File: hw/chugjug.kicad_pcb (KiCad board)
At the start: 4 copper layers, 50 x 50 mm, 42 parts, among them J1 SAMTEC_FTSH-107-01-L-DV-K-A, J2 BATT_IN_JST, J4 USB2.0 TYPE-C 6P SMD, U1 STM32U575RITxQ, U2 MCP73833-xxx-UN, U3 LIS3DH, U4 MAX98357A, U5 TPS78233DDCR

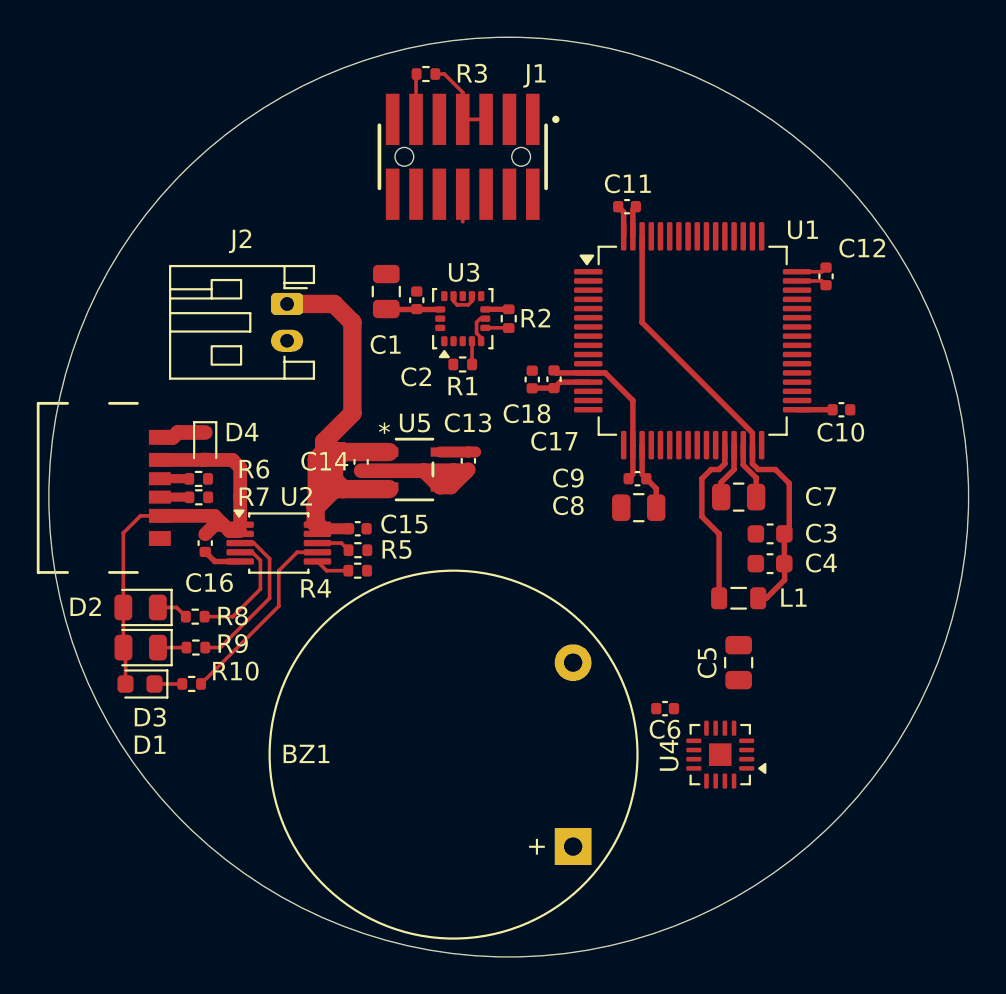
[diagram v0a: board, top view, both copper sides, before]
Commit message: much more layout changes. amp powered from +batt now
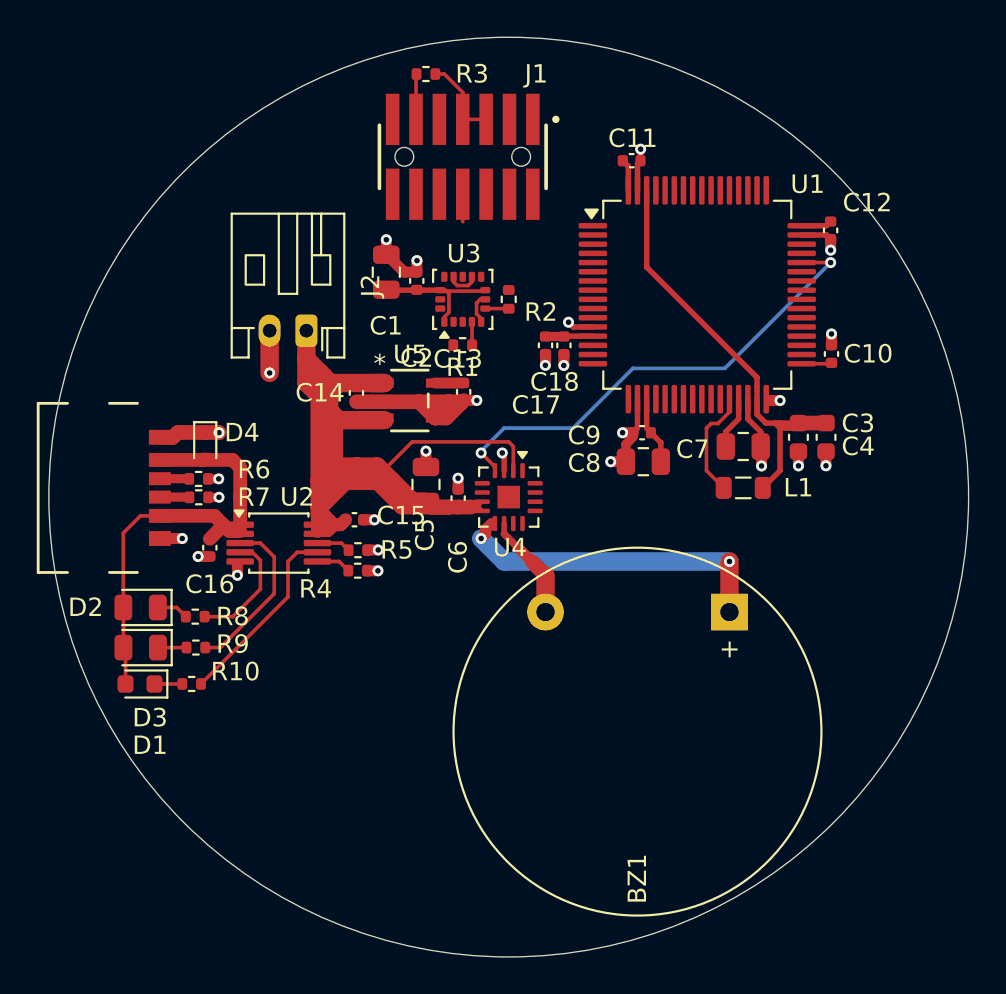
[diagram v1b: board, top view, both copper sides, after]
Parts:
- moved C5 19.6 mm to (145.5, 99.3)
- moved U4 18.1 mm to (150.0, 100.0), turned to -90 degrees
- moved C6 16.0 mm to (147.2, 100.1), turned to 90 degrees
- moved BZ1 15.3 mm to (162.0, 106.2), turned to 180 degrees
- moved C4 7.51 mm to (167.2, 96.8), turned to -90 degrees
- moved L1 6.01 mm to (162.8, 99.5)
- moved C3 5.47 mm to (165.8, 96.8), turned to -90 degrees
- moved C13 3.76 mm to (147.5, 94.3)
- moved C14 3.76 mm to (141.7, 94.3)
- moved U5 3.76 mm to (144.6, 94.8)
- moved C10 3.08 mm to (167.5, 92.2), turned to -90 degrees
- moved C7 2.76 mm to (162.8, 97.2)
- moved C18 2.53 mm to (153.0, 91.8), turned to 90 degrees
- moved C11 2.51 mm to (156.7, 81.7)
- moved C12 2.51 mm to (167.5, 85.5)
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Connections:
- C5 pad 1: 3V3 -> +BATT
- C5 pad 2: Net-(U4-GAIN_SLOT) -> GND
- C6 pad 1: 3V3 -> +BATT
- C6 pad 2: Net-(U4-GAIN_SLOT) -> GND
- U4 pad 2: Net-(U4-GAIN_SLOT) -> +BATT
- U4 pad 7: Net-(U4-GAIN_SLOT) -> +BATT
- U4 pad 8: Net-(U4-GAIN_SLOT) -> +BATT
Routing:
- net +BATT: track 29.9 -> 64.8 mm
- net /SD_MODE: track 0.00 -> 26.2 mm, vias 0 -> 2
- net Net-(BZ1-+): track 0.00 -> 18.1 mm, vias 0 -> 2
- net GND: track 38.4 -> 55.3 mm, vias 0 -> 28
- net Net-(BZ1--): track 0.00 -> 5.74 mm
- net /VLXSMPS: track 9.49 -> 5.95 mm
- net 3V3: track 21.0 -> 23.4 mm
- net /VDD11: track 24.5 -> 23.5 mm
- added copper zone on In2.Cu, net 3V3
- added copper zone on In1.Cu, net GND

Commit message: initial layout done
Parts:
- added REF**: MountingHole_2.2mm_M2, MountingHole:MountingHole_2.2mm_M2, F.Cu at (171.0, 96.2)
- added REF**: MountingHole_2.2mm_M2, MountingHole:MountingHole_2.2mm_M2, F.Cu at (131.2, 90.0)
- added REF**: MountingHole_2.2mm_M2, MountingHole:MountingHole_2.2mm_M2, F.Cu at (144.5, 120.8)
- moved R5 7.78 mm to (137.8, 96.2), turned to 180 degrees
- moved C16 5.46 mm to (135.2, 97.5), turned to 90 degrees
- moved U2 3.81 mm to (139.0, 99.0)
- moved C15 2.73 mm to (142.8, 98.8), turned to -90 degrees
- moved R4 2.56 mm to (141.2, 101.5), turned to 180 degrees
- moved R3 2.31 mm to (143.4, 77.8), turned to 90 degrees
- moved J1 1.60 mm to (148.8, 80.5)
- moved R2 1.05 mm to (149.9, 90.3), turned to 90 degrees
- moved R10 0.34 mm to (132.8, 110.5)
- moved D1 0.34 mm to (130.0, 110.5)
- moved C1 0.25 mm to (143.1, 87.8)
- moved C2 0.25 mm to (144.8, 88.2)
- moved D3 0.20 mm to (130.0, 108.4)
- moved R9 0.20 mm to (133.0, 108.4)
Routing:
- net /I2S_LRCLK: track 0.00 -> 27.8 mm, vias 0 -> 2
- net /STLINK_SWCLK: track 0.00 -> 24.8 mm, vias 0 -> 2
- net /LIS3DH_I2C1_SCL: track 1.27 -> 26.1 mm, vias 0 -> 2
- net /STLINK_SWO: track 1.50 -> 26.3 mm, vias 0 -> 2
- net /STLINK_SWDIO: track 0.00 -> 24.7 mm
- net /I2S_DATA: track 0.00 -> 24.0 mm, vias 0 -> 2
- net /LIS3DH_INT1: track 0.00 -> 22.2 mm, vias 0 -> 2
- net /I2S_BCLK: track 0.00 -> 22.0 mm, vias 0 -> 2
- net +BATT: track 64.8 -> 46.0 mm
- net /PWR_WKUP1: track 0.00 -> 17.8 mm
- net /STLINK_UART_RX: track 0.00 -> 17.4 mm, vias 0 -> 2
- net /LIS3DH_I2C1_SDA: track 1.28 -> 16.7 mm, vias 0 -> 2
- net /STLINK_UART_TX: track 0.00 -> 14.1 mm
- net /STLINK_NRST: track 0.00 -> 12.3 mm
- net 3V3: track 23.4 -> 35.5 mm, vias 0 -> 13
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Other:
- board text added: "CHG"
- board text added: "FULL"
- board text added: "PWR"

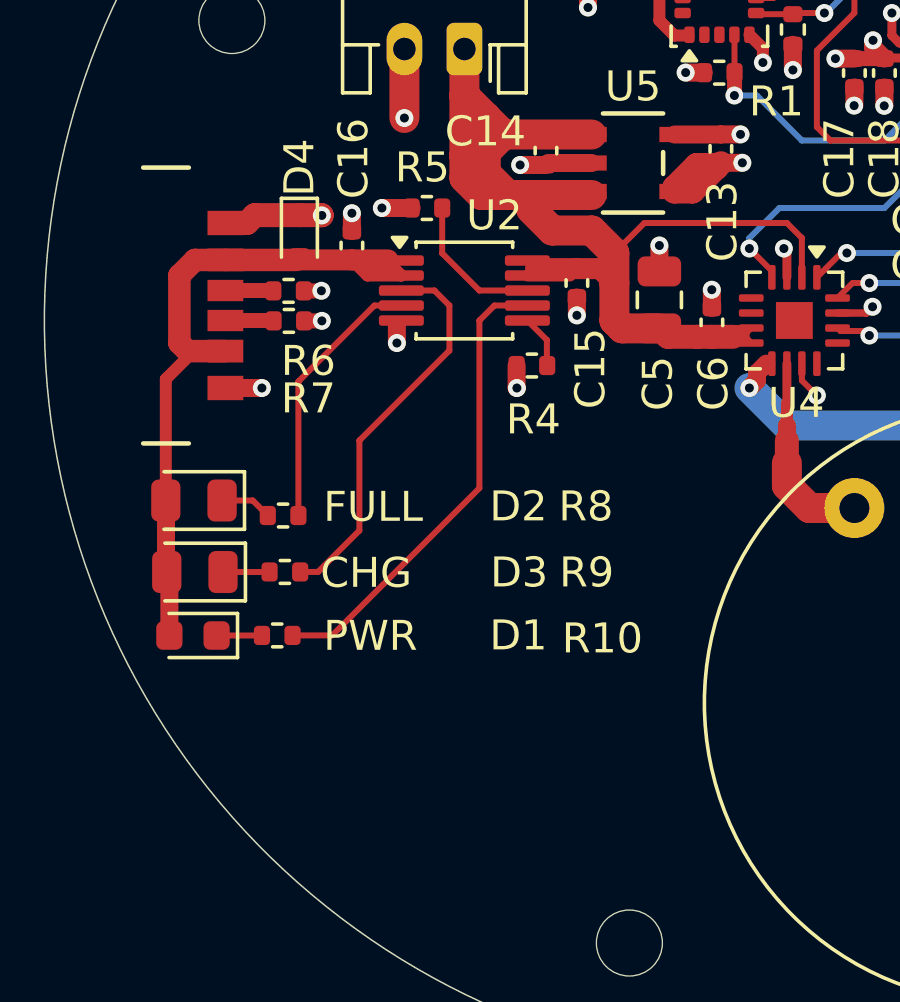
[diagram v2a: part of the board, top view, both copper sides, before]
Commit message: finalize pcb for jlcpcb ordering
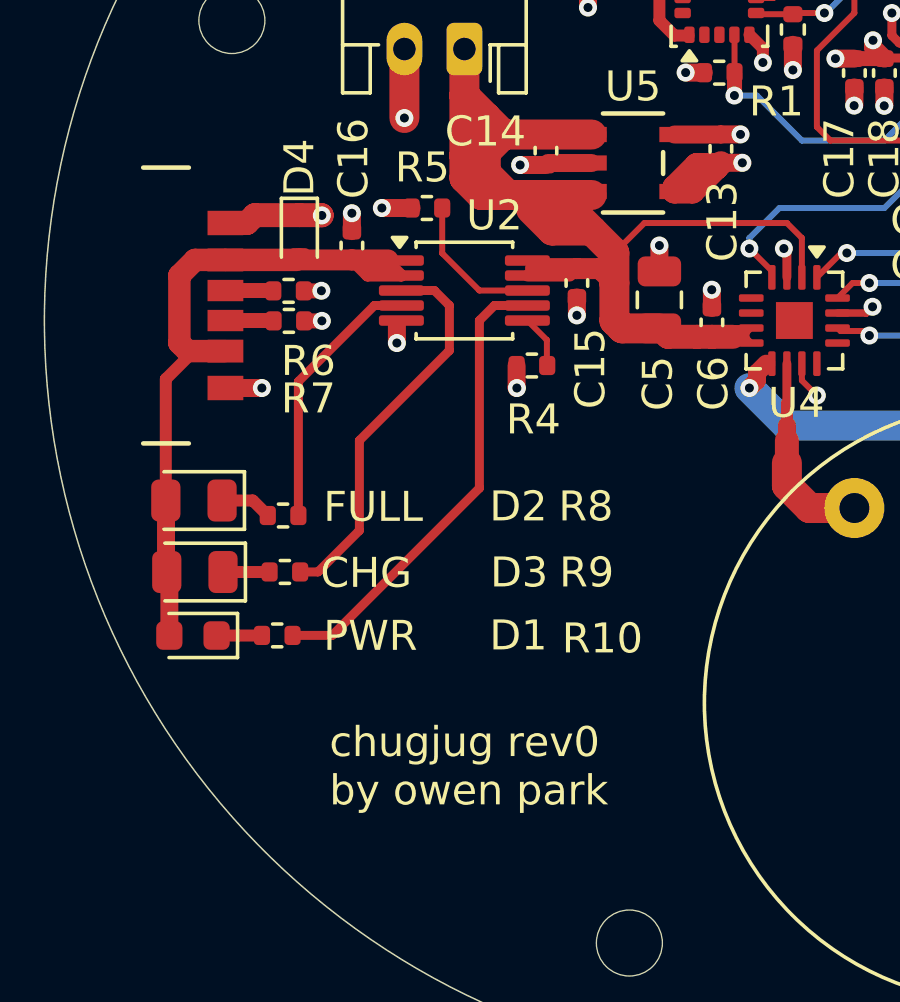
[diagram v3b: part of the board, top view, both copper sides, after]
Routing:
- net +BATT: track 46.0 -> 47.7 mm
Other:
- board text added: "chugjug rev0 by owen park"
